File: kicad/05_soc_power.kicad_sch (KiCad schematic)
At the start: 68 parts, among them U20 XC7Z020-2CLG484I

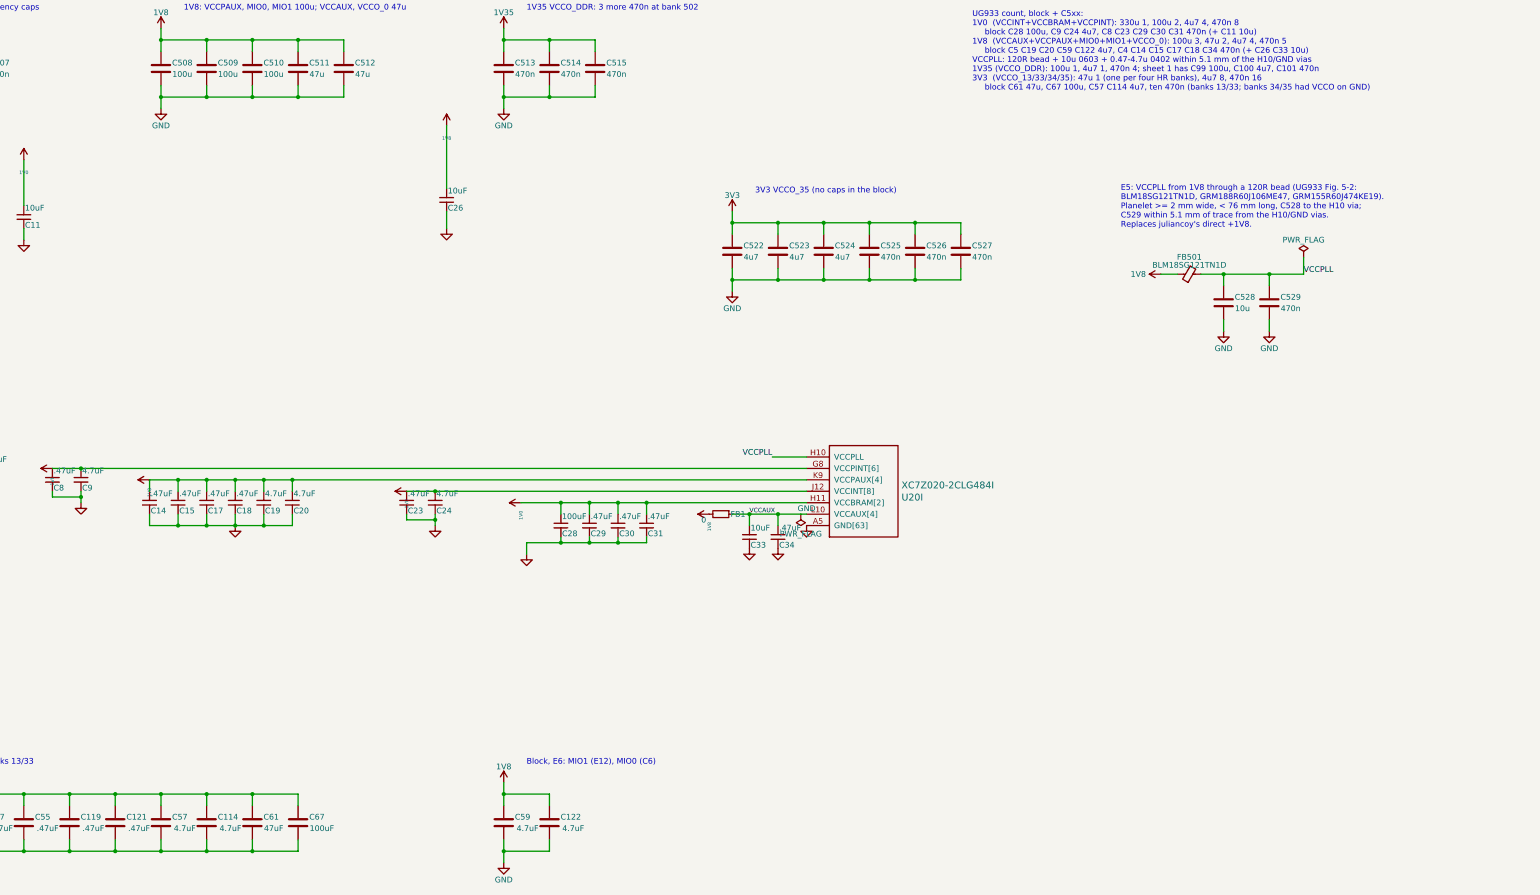
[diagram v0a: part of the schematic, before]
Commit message: Bottom-side heights checked (tools/check_heights.py), C67 22 uF 1206 (E12); RGMII TX series R at the SoC end
- tools/check_heights.py: the baseboard mapped through J11/J12, every card B.Cu part over a baseboard part within
  the 5.3 mm gap less 0.3 mm. C67 (100 uF 1210, 2.7 mm) over U17 (SOIC-16W) failed: now 22 uF 1206 CL31A226KAHNNNE
  (REUSE_LOG E12, user), 0.85 mm left; all pass. FP_SWAP in check_block_netlist.py, used by make_board/import_block.
  H1 push-pin barb over U17 fits (user).
- PHY area: TX series 22 R (R901-R906) moved from the PHY to B.Cu east of the block (sheet 9: TX at the SoC);
  R606 out of the eMMC ball field (placement/hand_fixes.sh).
- tools/sheets/_common.py: eeschema 10 sheets (no embedded_fonts) can be rebuilt again.
Checks: ERC 4 intended, block netlist and block copper 0 failures, DRC parity 0.

Co-Authored-By: Claude Opus 5.5 <noreply@anthropic.com>
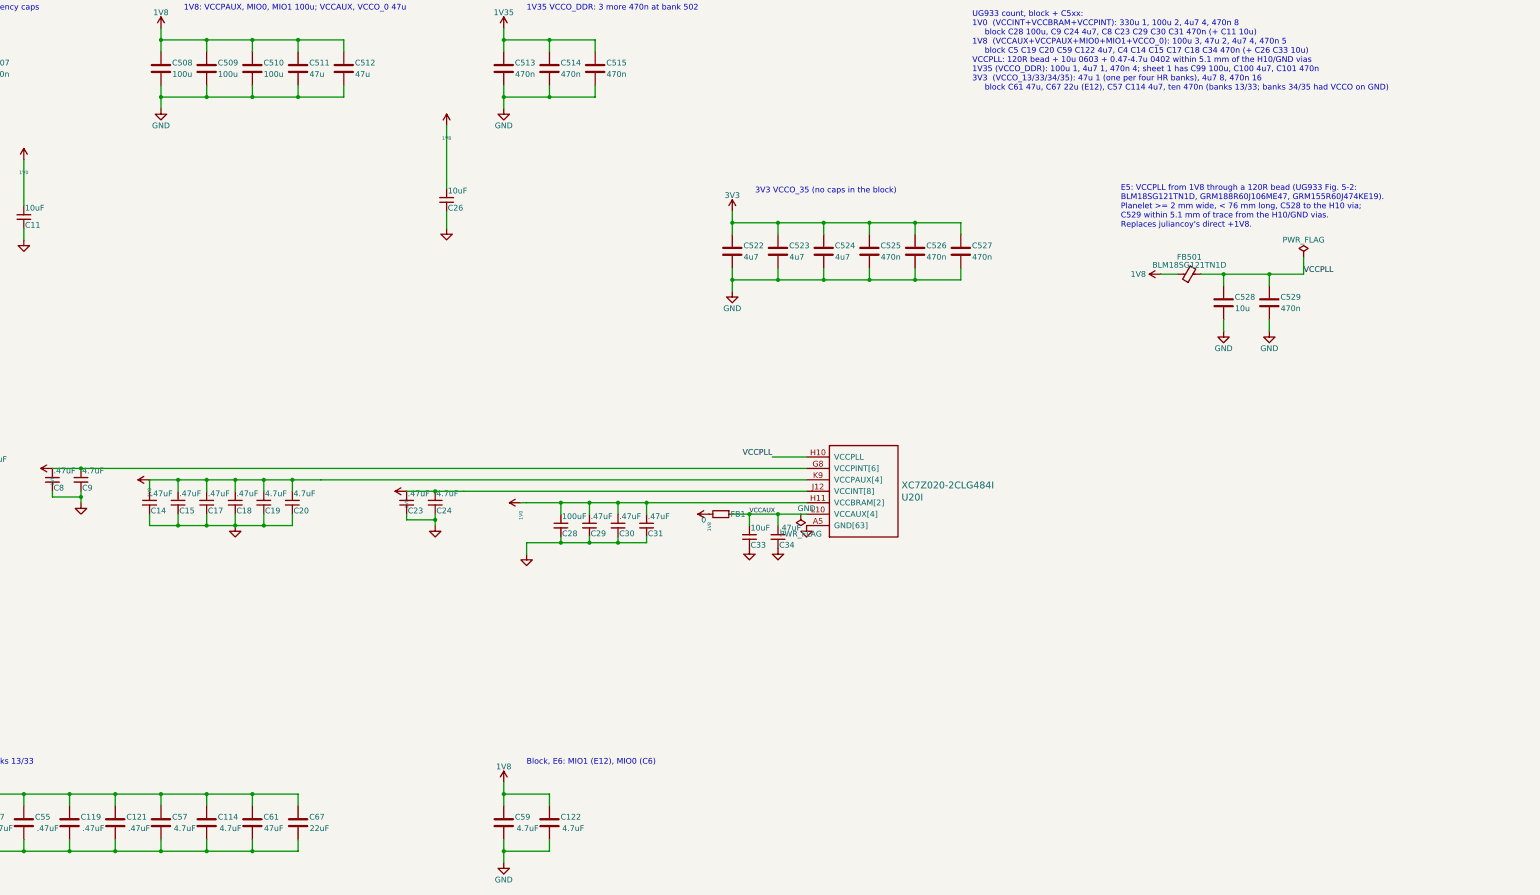
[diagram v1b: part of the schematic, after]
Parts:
- C67: value 100uF -> 22uF; footprint Capacitor_SMD:C_1210_3225Metric -> Capacitor_SMD:C_1206_3216Metric; LCSC C49066 -> C12891; MPN (none) -> CL31A226KAHNNNE
